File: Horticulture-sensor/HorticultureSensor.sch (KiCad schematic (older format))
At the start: 24 parts, among them J1 Conn_01x04, J2 Conn_02x05_Odd_Even, J3 Conn_01x03, J4 Conn_01x04, J5 Conn_01x03, J6 Conn_01x02, J7 Conn_01x02, J8 Conn_01x02, Q1 IRLML2030TRPBF, Q2 IRLML2030TRPBF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

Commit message: Resolves #4 #6 #5
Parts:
- removed C2: 1 uF, Capacitor_SMD:C_0805_2012Metric, symbol Device:C_Small
- removed J6, J7, J8: Conn_01x02, Connector_JST:JST_XH_B2B-XH-AM_1x02_P2.50mm_Vertical, symbol Connector_Generic:Conn_01x02
- removed JP1: SolderJumper_2_Open, Jumper:SolderJumper-2_P1.3mm_Open_RoundedPad1.0x1.5mm, symbol Jumper:SolderJumper_2_Open
- removed Q1, Q2: IRLML2030TRPBF, Package_TO_SOT_SMD:SOT-23, symbol Transistor_FET:IRLML0030
- removed R2: 10 kohm, Resistor_SMD:R_0805_2012Metric, symbol Device:R_Small
- removed U2: ENS210, Package_DFN_QFN:AMS_QFN-4-1EP_2x2mm_P0.95mm_EP0.7x1.6mm, symbol Sensor_Humidity:ENS210
- removed U3: MCP1700-3302E_TO, Package_TO_SOT_SMD:SOT-23, symbol Regulator_Linear:MCP1700-1202E_SOT23
- added J6: Conn_01x04, Connector_Molex:Molex_PicoBlade_53398-0471_1x04-1MP_P1.25mm_Vertical, symbol Connector_Generic:Conn_01x04
- C1: value 1 uF -> C_Small
- J1, J4: footprint Connector_JST:JST_XH_S4B-XH-A-1_1x04_P2.50mm_Horizontal -> Connector_Molex:Molex_PicoBlade_53398-0471_1x04-1MP_P1.25mm_Vertical
- J3, J5: footprint Connector_JST:JST_XH_B3B-XH-A_1x03_P2.50mm_Vertical -> Connector_Molex:Molex_PicoBlade_53398-0371_1x03-1MP_P1.25mm_Vertical
- R1: value 10 kohm -> R_Small
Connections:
- net +3V3: now also C1.1, R1.1
- net GND: now also J6.4 (Pin_4); no longer R1.2
- net VCC: now also J6.1 (Pin_1); no longer C1.1
- net nRESET: now also R1.2
- net mosfet0 renamed UART-rx
- net UART-rx: now also J6.3 (Pin_3); no longer R1.1
- net mosfet1 renamed UART-tx
- net UART-tx: now also J6.2 (Pin_2)

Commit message: Resolves #2
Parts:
- C1: value C_Small -> 100nF
- R1: value R_Small -> 10k2
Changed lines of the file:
@@
 P 7950 6950
 F 0 "C1" V 7721 6950 50  0000 C CNN
-F 1 "C_Small" V 7812 6950 50  0000 C CNN
+F 1 "100nF" V 7812 6950 50  0000 C CNN
 F 2 "Capacitor_SMD:C_0805_2012Metric" H 7950 6950 50  0001 C CNN
 F 3 "~" H 7950 6950 50  0001 C CNN
@@
 P 7650 6900
 F 0 "R1" H 7709 6946 50  0000 L CNN
-F 1 "R_Small" H 7709 6855 50  0000 L CNN
+F 1 "10k2" H 7709 6855 50  0000 L CNN
 F 2 "Resistor_SMD:R_0805_2012Metric" H 7650 6900 50  0001 C CNN
 F 3 "~" H 7650 6900 50  0001 C CNN
@@
 Connection ~ 8050 6950
 Connection ~ 8150 6950
-Wire Wire Line
-	8150 6950 8200 6950
 $Comp
 L power:GND #PWR0111

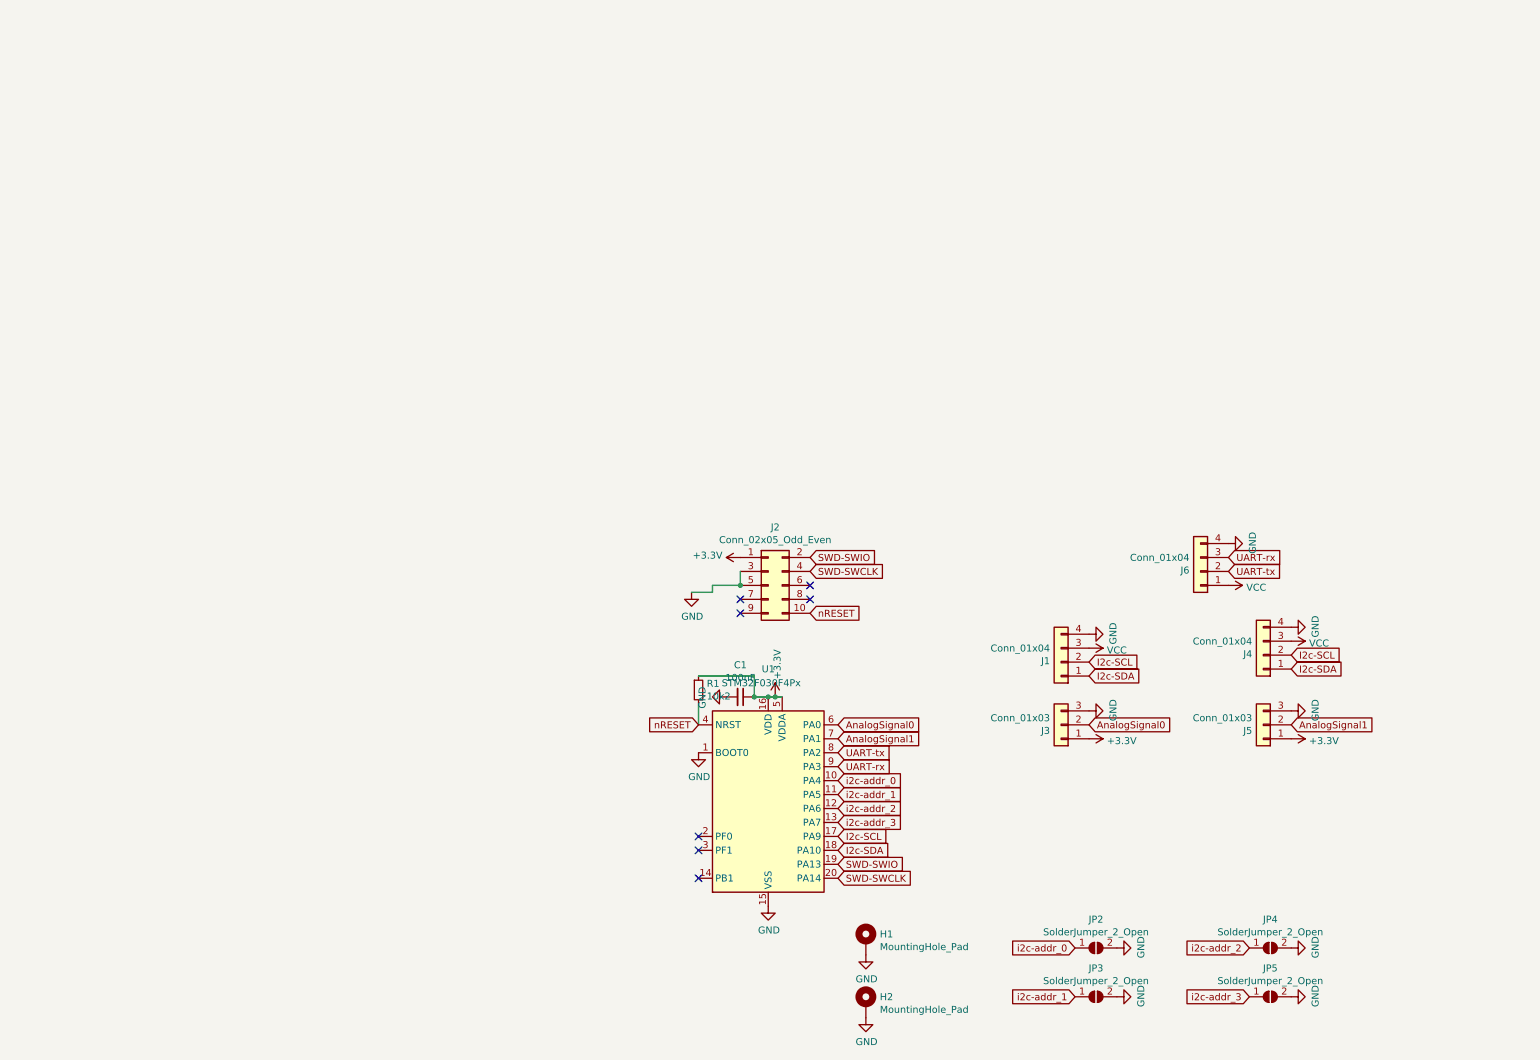
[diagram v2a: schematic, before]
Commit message: Completed routing
Soilsensor rev 1.0
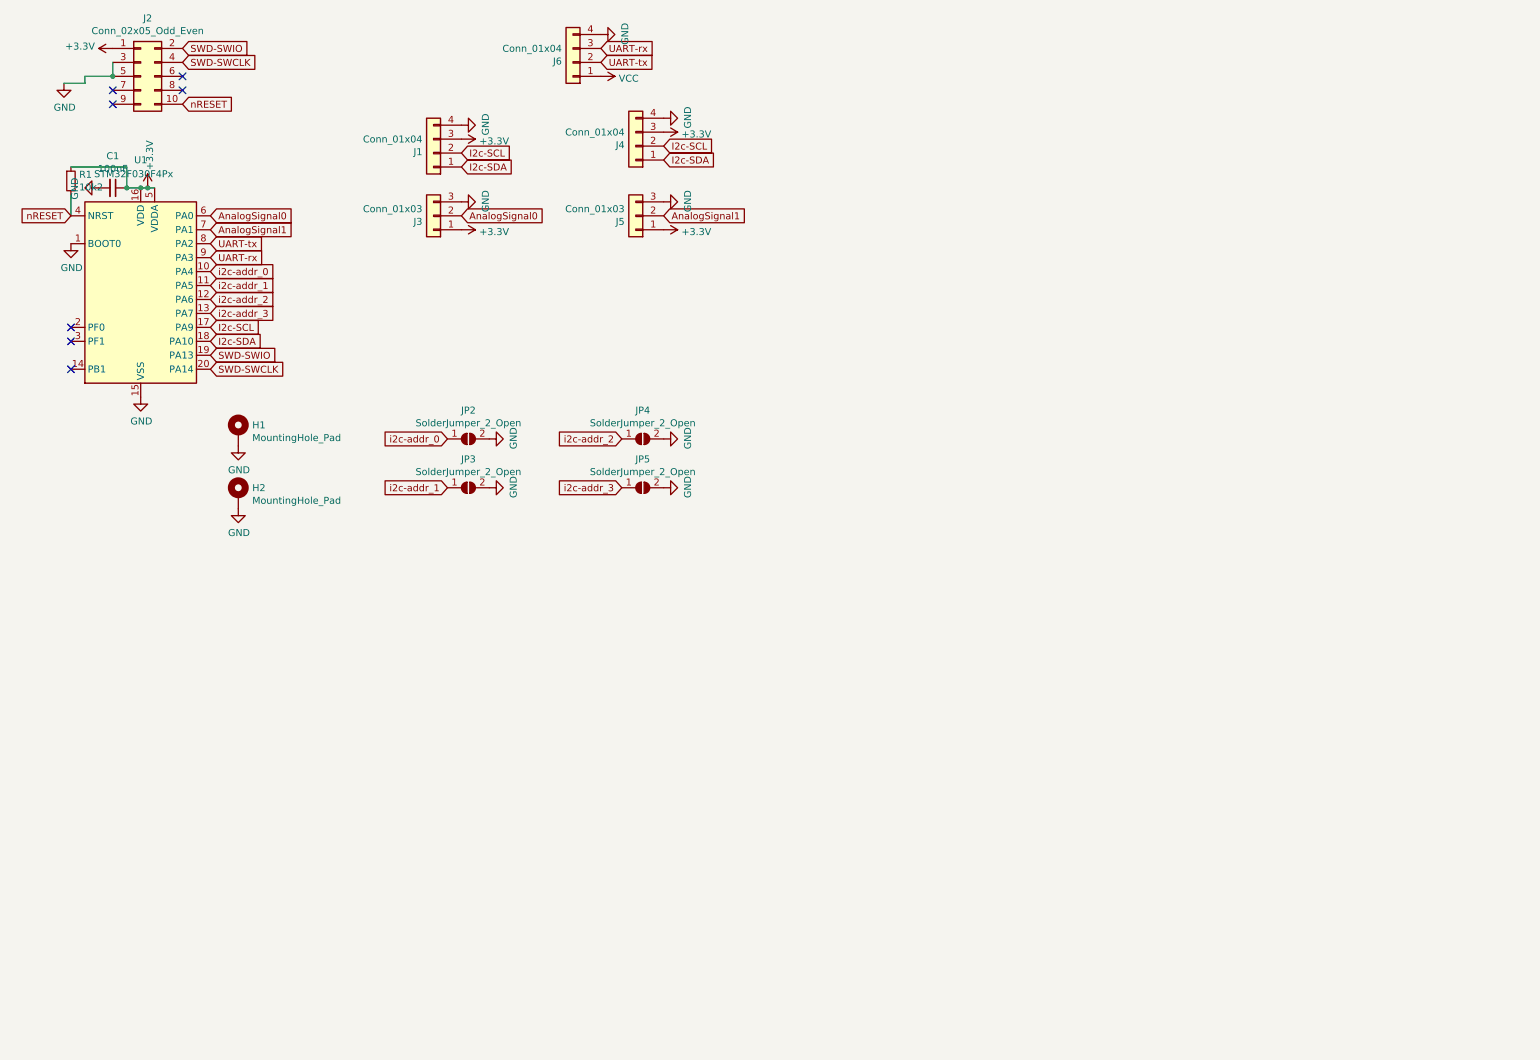
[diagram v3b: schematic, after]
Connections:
- net +3V3: now also J1.3 (Pin_3), J4.3 (Pin_3)
- net VCC: no longer J1.3 (Pin_3), J4.3 (Pin_3)
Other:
- moved on the sheet: C1, H1, H2, J1, J2, J3, J4, J5, J6, JP2, JP3, JP4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
